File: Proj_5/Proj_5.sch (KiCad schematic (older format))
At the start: 0 parts

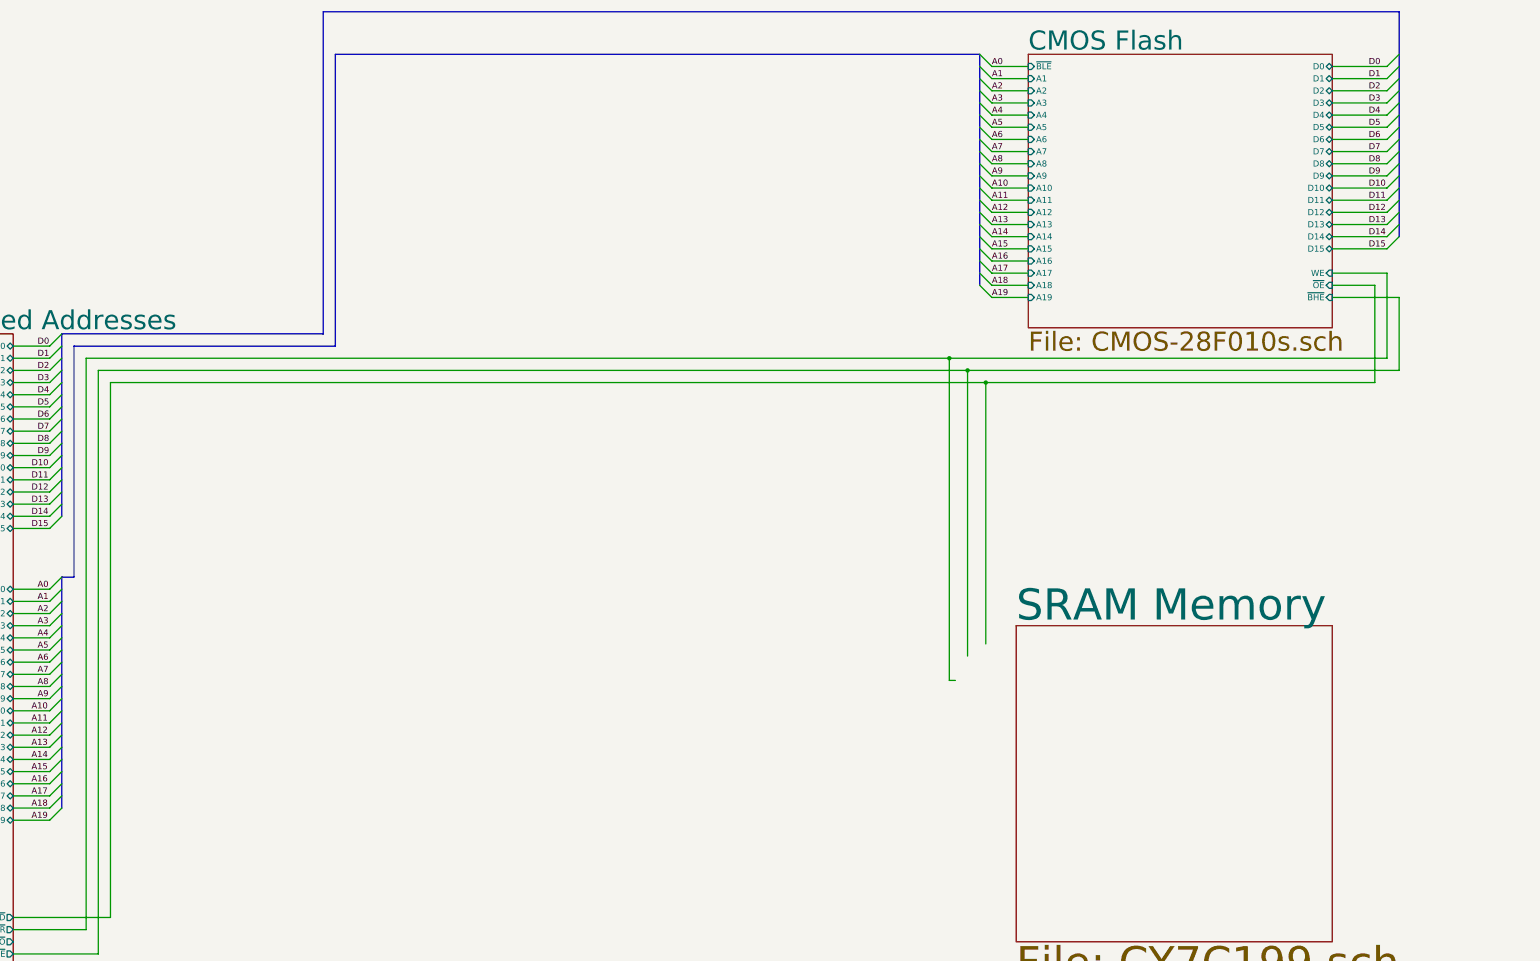
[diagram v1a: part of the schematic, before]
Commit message: Made the rest of the connections for the SRAM. Changed stuff on the main page
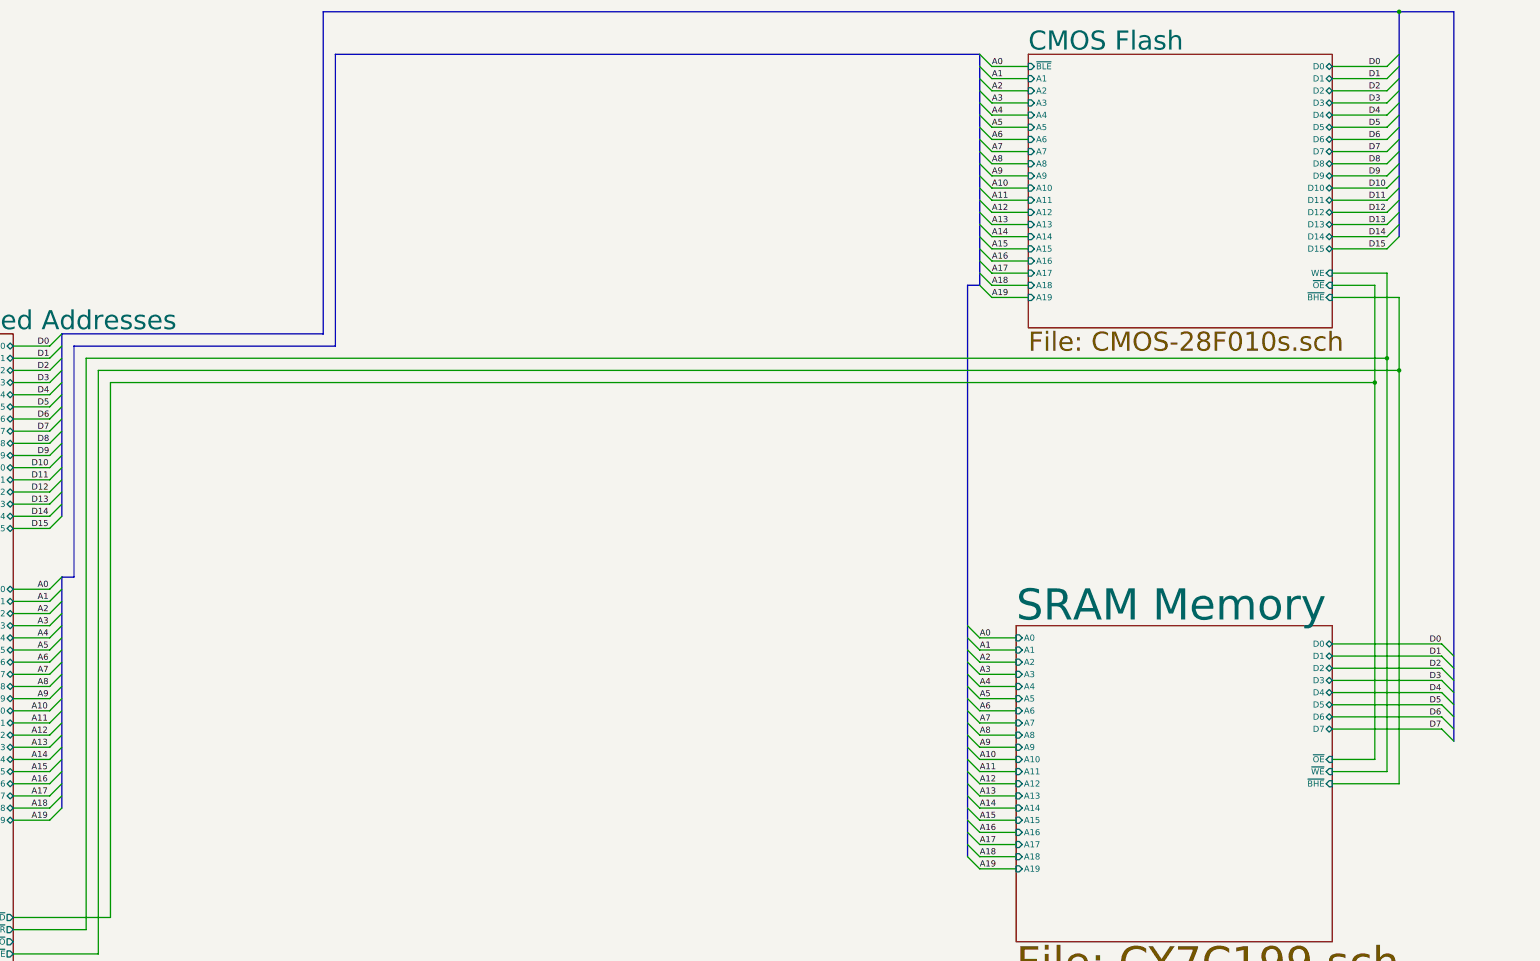
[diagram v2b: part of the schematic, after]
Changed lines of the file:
@@
 F0 "SRAM Memory" 256
 F1 "CY7C199.sch" 256
+F2 "A12" I L 24850 8600 50
+F3 "A15" I L 24850 8900 50
+F4 "A16" I L 24850 9000 50
+F5 "A11" I L 24850 8500 50
+F6 "A13" I L 24850 8700 50
+F7 "A14" I L 24850 8800 50
+F8 "A19" I L 24850 9300 50
+F9 "A18" I L 24850 9200 50
+F10 "A17" I L 24850 9100 50
+F11 "D3" B R 27450 7750 50
+F12 "D4" B R 27450 7850 50
+F13 "D5" B R 27450 7950 50
+F14 "D6" B R 27450 8050 50
+F15 "D7" B R 27450 8150 50
+F16 "D2" B R 27450 7650 50
+F17 "D1" B R 27450 7550 50
+F18 "D0" B R 27450 7450 50
+F19 "A0" I L 24850 7400 50
+F20 "A10" I L 24850 8400 50
+F21 "A9" I L 24850 8300 50
+F22 "A8" I L 24850 8200 50
+F23 "A7" I L 24850 8100 50
+F24 "A6" I L 24850 8000 50
+F25 "A5" I L 24850 7900 50
+F26 "A4" I L 24850 7800 50
+F27 "A3" I L 24850 7700 50
+F28 "A2" I L 24850 7600 50
+F29 "A1" I L 24850 7500 50
+F30 "~OE" I R 27450 8400 50
+F31 "~WE" I R 27450 8500 50
+F32 "~BHE" I R 27450 8600 50
 $EndSheet
 $Sheet
@@
 D15
 Wire Wire Line
-	27900 5100 24300 5100
-Wire Wire Line
 	17200 5100 17200 9800
 Wire Wire Line
@@
 Wire Wire Line
 	17300 10000 17300 5200
-Wire Wire Line
-	17300 5200 24450 5200
 Wire Wire Line
 	28000 5200 28000 4600
@@
 	27800 4500 27800 5300
 Wire Wire Line
-	27800 5300 24600 5300
-Wire Wire Line
 	17400 5300 17400 9700
 Wire Wire Line
 	17400 9700 16600 9700
-Wire Wire Line
-	24600 5300 24600 7450
-Connection ~ 24600 5300
-Wire Wire Line
-	24600 5300 17400 5300
-Wire Wire Line
-	24450 5200 24450 7550
-Connection ~ 24450 5200
-Wire Wire Line
-	24450 5200 28000 5200
-Wire Wire Line
-	24300 5100 24300 7750
-Wire Wire Line
-	24300 7750 24350 7750
-Connection ~ 24300 5100
-Wire Wire Line
-	24300 5100 17200 5100
 Wire Bus Line
 	19250 2600 24550 2600
@@
 F1 "8279_59_54.sch" 256
 $EndSheet
+Wire Wire Line
+	17400 5300 27800 5300
+Wire Wire Line
+	17300 5200 28000 5200
+Wire Wire Line
+	17200 5100 27900 5100
+Wire Wire Line
+	27800 5300 27800 8400
+Wire Wire Line
+	27800 8400 27450 8400
+Connection ~ 27800 5300
+Wire Wire Line
+	27900 5100 27900 8500
+Wire Wire Line
+	27900 8500 27450 8500
+Connection ~ 27900 5100
+Wire Wire Line
+	28000 8600 27450 8600
+Connection ~ 28000 5200
+Wire Bus Line
+	28000 2250 28450 2250
+Connection ~ 28000 2250
+Entry Wire Line
+	28450 7550 28350 7450
+Entry Wire Line
+	28450 7650 28350 7550
+Entry Wire Line
+	28450 7750 28350 7650
+Entry Wire Line
+	28450 7850 28350 7750
+Entry Wire Line
+	28450 7950 28350 7850
+Entry Wire Line
+	28450 8050 28350 7950
+Entry Wire Line
+	28450 8150 28350 8050
+Entry Wire Line
+	28450 8250 28350 8150
+Text Label 28250 7450 0    50   ~ 0
+D0
+Text Label 28250 7550 0    50   ~ 0
+D1
+Text Label 28250 7650 0    50   ~ 0
+D2
+Text Label 28250 7750 0    50   ~ 0
+D3
+Text Label 28250 7850 0    50   ~ 0
+D4
+Text Label 28250 7950 0    50   ~ 0
+D5
+Text Label 28250 8050 0    50   ~ 0
+D6
+Text Label 28250 8150 0    50   ~ 0
+D7
+Wire Wire Line
+	27450 7450 28350 7450
+Wire Wire Line
+	27450 7550 28350 7550
+Wire Wire Line
+	28000 5200 28000 8600
+Wire Wire Line
+	27450 7650 28350 7650
+Wire Wire Line
+	27450 7750 28350 7750
+Wire Wire Line
+	27450 7850 28350 7850
+Wire Wire Line
+	27450 7950 28350 7950
+Wire Wire Line
+	27450 8050 28350 8050
+Wire Wire Line
+	27450 8150 28350 8150
+Entry Wire Line
+	24450 9200 24550 9300
+Entry Wire Line
+	24450 9100 24550 9200
+Entry Wire Line
+	24450 9000 24550 9100
+Entry Wire Line
+	24450 8900 24550 9000
+Entry Wire Line
+	24450 8800 24550 8900
+Entry Wire Line
+	24450 8700 24550 8800
+Entry Wire Line
+	24450 8600 24550 8700
+Entry Wire Line
+	24450 8500 24550 8600
+Entry Wire Line
+	24450 8400 24550 8500
+Entry Wire Line
+	24450 8300 24550 8400
+Entry Wire Line
+	24450 8200 24550 8300
+Entry Wire Line
+	24450 8100 24550 8200
+Entry Wire Line
+	24450 8000 24550 8100
+Entry Wire Line
+	24450 7900 24550 8000
+Entry Wire Line
+	24450 7800 24550 7900
+Entry Wire Line
+	24450 7700 24550 7800
+Entry Wire Line
+	24450 7600 24550 7700
+Entry Wire Line
+	24450 7300 24550 7400
+Wire Wire Line
+	24550 7700 24850 7700
+Wire Wire Line
+	24550 7800 24850 7800
+Wire Wire Line
+	24550 7900 24850 7900
+Wire Wire Line
+	24550 8000 24850 8000
+Wire Wire Line
+	24550 8100 24850 8100
+Wire Wire Line
+	24550 8200 24850 8200
+Wire Wire Line
+	24550 8300 24850 8300
+Wire Wire Line
+	24550 8400 24850 8400
+Wire Wire Line
+	24550 8500 24850 8500
+Wire Wire Line
+	24550 8600 24850 8600
+Wire Wire Line
+	24550 8700 24850 8700
+Wire Wire Line
+	24550 8800 24850 8800
+Wire Wire Line
+	24550 8900 24850 8900
+Wire Wire Line
+	24550 9000 24850 9000
+Wire Wire Line
+	24550 9100 24850 9100
+Wire Wire Line
+	24550 9200 24850 9200
+Wire Wire Line
+	24550 9300 24850 9300
+Text Label 24550 7400 0    50   ~ 0
+A0
+Text Label 24550 7800 0    50   ~ 0
+A4
+Text Label 24550 7900 0    50   ~ 0
+A5
+Text Label 24550 8000 0    50   ~ 0
+A6
+Text Label 24550 8100 0    50   ~ 0
+A7
+Text Label 24550 8200 0    50   ~ 0
+A8
+Text Label 24550 8300 0    50   ~ 0
+A9
+Text Label 24550 8400 0    50   ~ 0
+A10
+Text Label 24550 8500 0    50   ~ 0
+A11
+Text Label 24550 8600 0    50   ~ 0
+A12
+Text Label 24550 8700 0    50   ~ 0
+A13
+Text Label 24550 8800 0    50   ~ 0
+A14
+Text Label 24550 8900 0    50   ~ 0
+A15
+Text Label 24550 9000 0    50   ~ 0
+A16
+Text Label 24550 9100 0    50   ~ 0
+A17
+Text Label 24550 9200 0    50   ~ 0
+A18
+Text Label 24550 9300 0    50   ~ 0
+A19
+Text Label 24550 7700 0    50   ~ 0
+A3
+Wire Wire Line
+	24550 7400 24850 7400
+Entry Wire Line
+	24450 7400 24550 7500
+Entry Wire Line
+	24450 7500 24550 7600
+Wire Wire Line
+	24550 7500 24850 7500
+Wire Wire Line
+	24550 7600 24850 7600
+Text Label 24550 7500 0    50   ~ 0
+A1
+Text Label 24550 7600 0    50   ~ 0
+A2
+Wire Bus Line
+	24450 4500 24550 4500
+Wire Bus Line
+	28450 2250 28450 8250
 Wire Bus Line
 	17000 4900 17000 6400
@@
 	17000 6900 17000 8800
 Wire Bus Line
+	24450 4500 24450 9200
+Wire Bus Line
 	24550 2600 24550 4500

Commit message: Rerouted Ext Wires, UART Mostly Complete, All Headers Added
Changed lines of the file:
@@
 F33 "M~IO" I R 27450 8900 50
-$EndSheet
-$Sheet
-S 14000 12600 2450 2500
-U 5EA98A67
-F0 "16550 UART" 256
-F1 "16550UART.sch" 256
 $EndSheet
 Text Notes 28400 22050 0    169  ~ 0
@@
 F0 "8279, 8259, 8254" 256
 F1 "8279_59_54.sch" 256
-F2 "RESET" O R 8100 5250 50
-F3 "NMI" O R 8100 5150 50
-F4 "D7" B R 8100 1950 50
-F5 "D6" B R 8100 2100 50
-F6 "D5" B R 8100 2250 50
-F7 "D4" B R 8100 2400 50
-F8 "D3" B R 8100 2550 50
-F9 "D2" B R 8100 2700 50
-F10 "D1" B R 8100 2850 50
-F11 "D0" B R 8100 3000 50
-F12 "~WR" I R 8100 3900 50
-F13 "~RD" I R 8100 3800 50
-F14 "MAIN_CLK" I R 8100 4200 50
+F2 "NMI" O R 8100 5150 50
+F3 "D7" B R 8100 1950 50
+F4 "D6" B R 8100 2100 50
+F5 "D5" B R 8100 2250 50
+F6 "D4" B R 8100 2400 50
+F7 "D3" B R 8100 2550 50
+F8 "D2" B R 8100 2700 50
+F9 "D1" B R 8100 2850 50
+F10 "D0" B R 8100 3000 50
+F11 "MAIN_CLK" I R 8100 4200 50
+F12 "IR3" O L 3450 4900 50
+F13 "~WR" I L 3450 2600 50
+F14 "~RD" I L 3450 2700 50
+F15 "RESET" O R 8100 3900 50
 $EndSheet
 $Sheet
@@
 F42 "CLK" I L 14100 5000 50
 F43 "RESET" I L 14100 5150 50
+F44 "INTR" I L 14100 6350 50
 $EndSheet
 Text Label 19250 6150 0    118  ~ 0
@@
 Entry Wire Line
 	16850 10000 16950 10100
-Wire Wire Line
-	10950 13950 7150 13950
 Wire Bus Line
 	16950 10250 17450 10250
@@
 Text Label 28900 4700 2    50   ~ 0
 M~IO
-Wire Bus Line
-	29100 1250 9100 1250
-Wire Bus Line
-	9100 1250 9100 3850
 Entry Wire Line
 	8600 1950 8700 2050
@@
 Wire Wire Line
 	8100 2700 8600 2700
-Wire Wire Line
-	8100 3800 8950 3800
-Wire Wire Line
-	8100 3900 8950 3900
-Entry Wire Line
-	8950 3800 9050 3900
-Entry Wire Line
-	8950 3900 9050 4000
-Wire Bus Line
-	9100 3850 9050 3850
-Text Label 8750 3800 2    50   ~ 0
-~RD
-Text Label 8750 3900 2    50   ~ 0
-~WR
 Wire Bus Line
 	17450 10250 17450 11350
@@
 	7650 13500 7750 13600
 Wire Wire Line
-	14000 4200 8100 4200
+	14000 4200 11200 4200
 Wire Wire Line
 	14000 3200 14000 4200
@@
 	14800 2650 9350 2650
 Wire Wire Line
-	9350 2650 9350 5250
-Wire Wire Line
-	9350 5250 8100 5250
+	9350 2650 9350 3900
 Wire Wire Line
 	14800 2950 13650 2950
@@
 	13650 5150 14100 5150
 Wire Wire Line
-	13650 5150 10950 5150
-Wire Wire Line
-	10950 5150 10950 13950
+	13650 5150 13650 13950
 Connection ~ 13650 5150
-Wire Bus Line
-	9050 3850 9050 4000
+Wire Wire Line
+	3450 4900 3400 4900
+$Sheet
+S 4400 7300 2450 2500
+U 5EA98A67
+F0 "16550 UART" 256
+F1 "16550UART.sch" 256
+F2 "MAIN_CLOCK" I R 6850 7600 50
+F3 "IR3" I L 4400 7500 50
+F4 "~WR" I L 4400 7950 50
+F5 "~RD" I L 4400 8050 50
+F6 "D7" B R 6850 9600 50
+F7 "D6" B R 6850 9500 50
+F8 "D5" B R 6850 9400 50
+F9 "D4" B R 6850 9300 50
+F10 "D3" B R 6850 9200 50
+F11 "D2" B R 6850 9100 50
+F12 "D1" B R 6850 9000 50
+F13 "D0" B R 6850 8900 50
+$EndSheet
+Wire Wire Line
+	7150 13950 13650 13950
+Text Label 2800 2700 0    50   ~ 0
+~RD
+Text Label 2800 2600 0    50   ~ 0
+~WR
+Wire Wire Line
+	3450 2700 2550 2700
+Wire Wire Line
+	3450 2600 2550 2600
+Entry Wire Line
+	2550 2700 2450 2600
+Entry Wire Line
+	2550 2600 2450 2500
+Wire Bus Line
+	2450 1250 29100 1250
+Wire Wire Line
+	8100 3900 9350 3900
+Text Label 3750 8050 0    50   ~ 0
+~RD
+Text Label 3750 7950 0    50   ~ 0
+~WR
+Wire Wire Line
+	4400 8050 3500 8050
+Wire Wire Line
+	4400 7950 3500 7950
+Entry Wire Line
+	3500 8050 3400 7950
+Entry Wire Line
+	3500 7950 3400 7850
+Wire Bus Line
+	2450 7650 3400 7650
+Wire Wire Line
+	3400 4900 3400 6050
+Wire Wire Line
+	3400 6050 4350 6050
+Wire Wire Line
+	4350 6050 4350 7500
+Wire Wire Line
+	4350 7500 4400 7500
+Wire Wire Line
+	13450 5150 13450 6350
+Wire Wire Line
+	13450 6350 14100 6350
+Wire Wire Line
+	8100 5150 13450 5150
+Wire Wire Line
+	6850 7600 11200 7600
+Wire Wire Line
+	11200 7600 11200 4200
+Connection ~ 11200 4200
+Wire Wire Line
+	11200 4200 8100 4200
+Entry Wire Line
+	7200 9000 7100 8900
+Entry Wire Line
+	7200 9100 7100 9000
+Entry Wire Line
+	7200 9200 7100 9100
+Entry Wire Line
+	7200 9300 7100 9200
+Entry Wire Line
+	7200 9400 7100 9300
+Entry Wire Line
+	7200 9500 7100 9400
+Entry Wire Line
+	7200 9600 7100 9500
+Entry Wire Line
+	7200 9700 7100 9600
+Text Label 7000 8900 0    50   ~ 0
+D0
+Text Label 7000 9000 0    50   ~ 0
+D1
+Text Label 7000 9100 0    50   ~ 0
+D2
+Text Label 7000 9200 0    50   ~ 0
+D3
+Text Label 7000 9300 0    50   ~ 0
+D4
+Text Label 7000 9400 0    50   ~ 0
+D5
+Text Label 7000 9500 0    50   ~ 0
+D6
+Text Label 7000 9600 0    50   ~ 0
+D7
+Wire Wire Line
+	7100 8900 6850 8900
+Wire Wire Line
+	7100 9000 6850 9000
+Wire Wire Line
+	7100 9100 6850 9100
+Wire Wire Line
+	7100 9200 6850 9200
+Wire Wire Line
+	7100 9300 6850 9300
+Wire Wire Line
+	7100 9400 6850 9400
+Wire Wire Line
+	7100 9500 6850 9500
+Wire Wire Line
+	7100 9600 6850 9600
+Wire Bus Line
+	7500 11450 7500 9800
+Wire Bus Line
+	7500 9800 7200 9800
+Connection ~ 7500 11450
+Wire Bus Line
+	3400 7650 3400 7950
 Wire Bus Line
 	7750 11350 7750 13600
 Wire Bus Line
+	2450 1250 2450 7650
+Wire Bus Line
 	16950 9800 16950 10250
 Wire Bus Line
@@
 	28450 2250 28450 8250
 Wire Bus Line
+	7200 9000 7200 9800
+Wire Bus Line
 	17000 4900 17000 6400

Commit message: Monch
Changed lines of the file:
@@
 	13650 5150 14100 5150
 Wire Wire Line
-	13650 5150 13650 13950
+	13650 5150 13650 11250
 Connection ~ 13650 5150
 Wire Wire Line
 	3450 4900 3400 4900
-$Sheet
-S 4400 7300 2450 2500
-U 5EA98A67
-F0 "16550 UART" 256
-F1 "16550UART.sch" 256
-F2 "MAIN_CLOCK" I R 6850 7600 50
-F3 "IR3" I L 4400 7500 50
-F4 "~WR" I L 4400 7950 50
-F5 "~RD" I L 4400 8050 50
-F6 "D7" B R 6850 9600 50
-F7 "D6" B R 6850 9500 50
-F8 "D5" B R 6850 9400 50
-F9 "D4" B R 6850 9300 50
-F10 "D3" B R 6850 9200 50
-F11 "D2" B R 6850 9100 50
-F12 "D1" B R 6850 9000 50
-F13 "D0" B R 6850 8900 50
-$EndSheet
 Wire Wire Line
 	7150 13950 13650 13950
@@
 	7500 9800 7200 9800
 Connection ~ 7500 11450
+$Sheet
+S 4400 7300 2450 3250
+U 5EA98A67
+F0 "16550 UART" 256
+F1 "16550UART.sch" 256
+F2 "MAIN_CLOCK" I R 6850 7600 50
+F3 "IR3" I L 4400 7500 50
+F4 "~WR" I L 4400 7950 50
+F5 "~RD" I L 4400 8050 50
+F6 "D7" B R 6850 9600 50
+F7 "D6" B R 6850 9500 50
+F8 "D5" B R 6850 9400 50
+F9 "D4" B R 6850 9300 50
+F10 "D3" B R 6850 9200 50
+F11 "D2" B R 6850 9100 50
+F12 "D1" B R 6850 9000 50
+F13 "D0" B R 6850 8900 50
+F14 "RESET" I L 4400 7850 50
+F15 "A1" I L 4400 8350 50
+F16 "A2" I L 4400 8450 50
+F17 "A3" I L 4400 8550 50
+F18 "A4" I L 4400 8650 50
+F19 "A5" I L 4400 8750 50
+F20 "A6" I L 4400 8850 50
+F21 "A7" I L 4400 8950 50
+F22 "A8" I L 4400 9050 50
+F23 "A9" I L 4400 9150 50
+F24 "A10" I L 4400 9250 50
+F25 "A11" I L 4400 9350 50
+F26 "A12" I L 4400 9450 50
+F27 "A13" I L 4400 9550 50
+F28 "A14" I L 4400 9650 50
+F29 "A15" I L 4400 9750 50
+F30 "A0" I L 4400 8250 50
+F31 "A16" I L 4400 9850 50
+F32 "A17" I L 4400 9950 50
+F33 "A18" I L 4400 10050 50
+F34 "A19" I L 4400 10150 50
+$EndSheet
+Entry Wire Line
+	4000 10050 4100 10150
+Entry Wire Line
+	4000 9950 4100 10050
+Entry Wire Line
+	4000 9850 4100 9950
+Entry Wire Line
+	4000 9750 4100 9850
+Entry Wire Line
+	4000 9650 4100 9750
+Entry Wire Line
+	4000 9550 4100 9650
+Entry Wire Line
+	4000 9450 4100 9550
+Entry Wire Line
+	4000 9350 4100 9450
+Entry Wire Line
+	4000 9250 4100 9350
+Entry Wire Line
+	4000 9150 4100 9250
+Entry Wire Line
+	4000 9050 4100 9150
+Entry Wire Line
+	4000 8950 4100 9050
+Entry Wire Line
+	4000 8850 4100 8950
+Entry Wire Line
+	4000 8750 4100 8850
+Entry Wire Line
+	4000 8650 4100 8750
+Entry Wire Line
+	4000 8550 4100 8650
+Entry Wire Line
+	4000 8450 4100 8550
+Entry Wire Line
+	4000 8150 4100 8250
+Wire Wire Line
+	4100 8550 4400 8550
+Wire Wire Line
+	4100 8650 4400 8650
+Wire Wire Line
+	4100 8750 4400 8750
+Wire Wire Line
+	4100 8850 4400 8850
+Wire Wire Line
+	4100 8950 4400 8950
+Wire Wire Line
+	4100 9050 4400 9050
+Wire Wire Line
+	4100 9150 4400 9150
+Wire Wire Line
+	4100 9250 4400 9250
+Wire Wire Line
+	4100 9350 4400 9350
+Wire Wire Line
+	4100 9450 4400 9450
+Wire Wire Line
+	4100 9550 4400 9550
+Wire Wire Line
+	4100 9650 4400 9650
+Wire Wire Line
+	4100 9750 4400 9750
+Wire Wire Line
+	4100 9850 4400 9850
+Wire Wire Line
+	4100 9950 4400 9950
+Wire Wire Line
+	4100 10050 4400 10050
+Wire Wire Line
+	4100 10150 4400 10150
+Text Label 4100 8250 0    50   ~ 0
+A0
+Text Label 4100 8650 0    50   ~ 0
+A4
+Text Label 4100 8750 0    50   ~ 0
+A5
+Text Label 4100 8850 0    50   ~ 0
+A6
+Text Label 4100 8950 0    50   ~ 0
+A7
+Text Label 4100 9050 0    50   ~ 0
+A8
+Text Label 4100 9150 0    50   ~ 0
+A9
+Text Label 4100 9250 0    50   ~ 0
+A10
+Text Label 4100 9350 0    50   ~ 0
+A11
+Text Label 4100 9450 0    50   ~ 0
+A12
+Text Label 4100 9550 0    50   ~ 0
+A13
+Text Label 4100 9650 0    50   ~ 0
+A14
+Text Label 4100 9750 0    50   ~ 0
+A15
+Text Label 4100 9850 0    50   ~ 0
+A16
+Text Label 4100 9950 0    50   ~ 0
+A17
+Text Label 4100 10050 0    50   ~ 0
+A18
+Text Label 4100 10150 0    50   ~ 0
+A19
+Text Label 4100 8550 0    50   ~ 0
+A3
+Wire Wire Line
+	4100 8250 4400 8250
+Entry Wire Line
+	4000 8250 4100 8350
+Entry Wire Line
+	4000 8350 4100 8450
+Wire Wire Line
+	4100 8350 4400 8350
+Wire Wire Line
+	4100 8450 4400 8450
+Text Label 4100 8350 0    50   ~ 0
+A1
+Text Label 4100 8450 0    50   ~ 0
+A2
+Wire Bus Line
+	4250 11550 4000 11550
+Connection ~ 4250 11550
+Wire Wire Line
+	13650 11250 3600 11250
+Wire Wire Line
+	3600 11250 3600 7850
+Wire Wire Line
+	3600 7850 4400 7850
 Wire Bus Line
 	3400 7650 3400 7950
@@
 	16950 9800 16950 10250
 Wire Bus Line
+	7200 9000 7200 9800
+Wire Bus Line
 	8700 1750 8700 3100
 Wire Bus Line
@@
 	28450 2250 28450 8250
 Wire Bus Line
-	7200 9000 7200 9800
-Wire Bus Line
 	17000 4900 17000 6400
 Wire Bus Line
@@
 Wire Bus Line
 	4250 11550 4250 14100
+Wire Bus Line
+	4000 8150 4000 11550
+Connection ~ 13650 11250
+Wire Wire Line
+	13650 11250 13650 13950
 $EndSCHEMATC
